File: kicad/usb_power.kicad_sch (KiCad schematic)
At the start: 12 parts, among them J1 12402012E212A, U6 TLV73333PDBV, U7 TLV73325PDBV

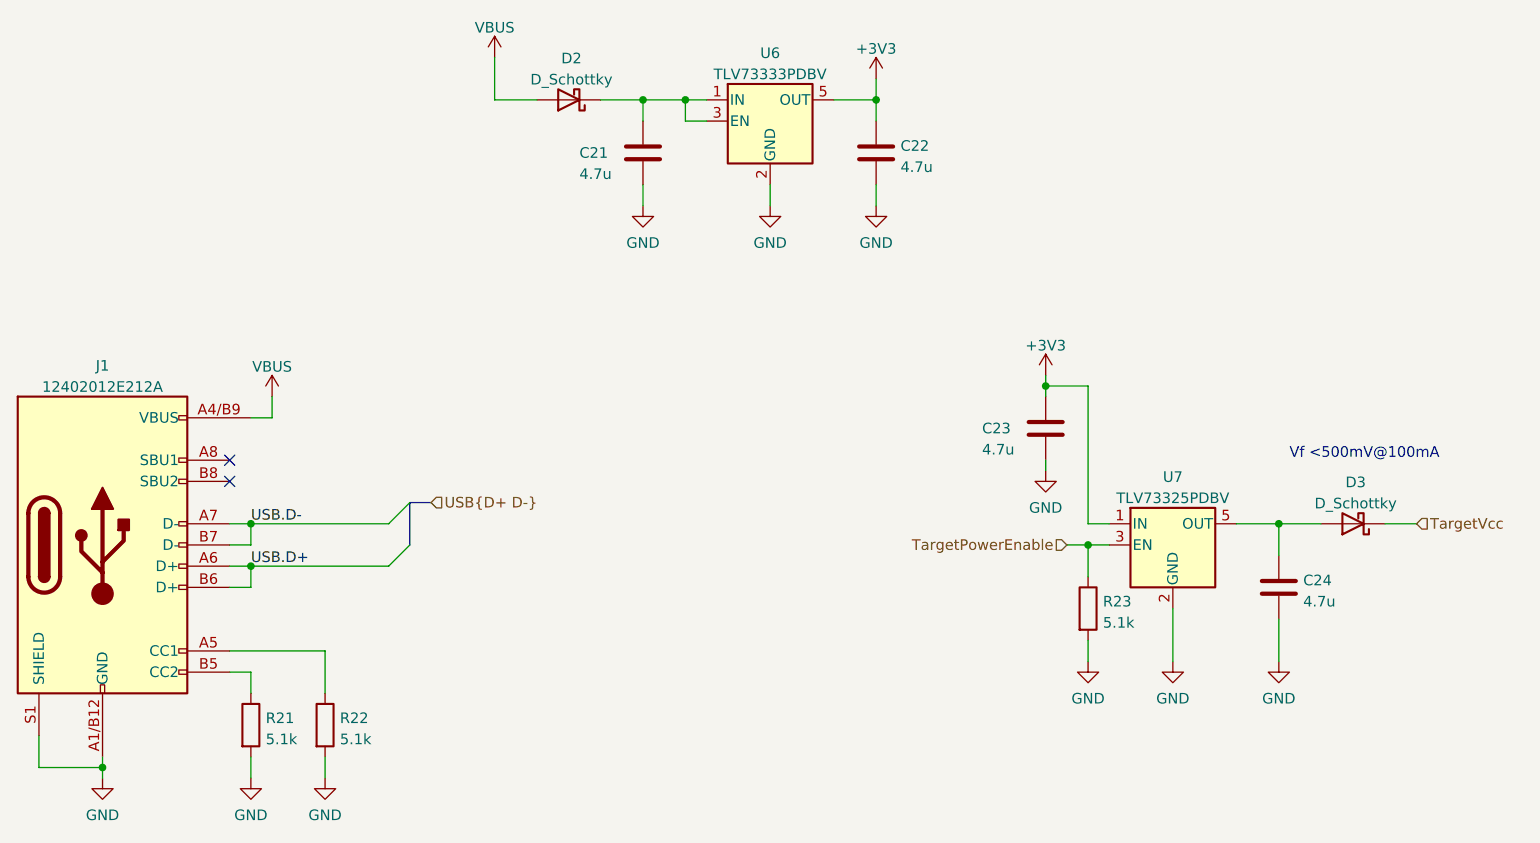
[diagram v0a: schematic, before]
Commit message: add fourth level converter for simultaneous programming + TX/RX
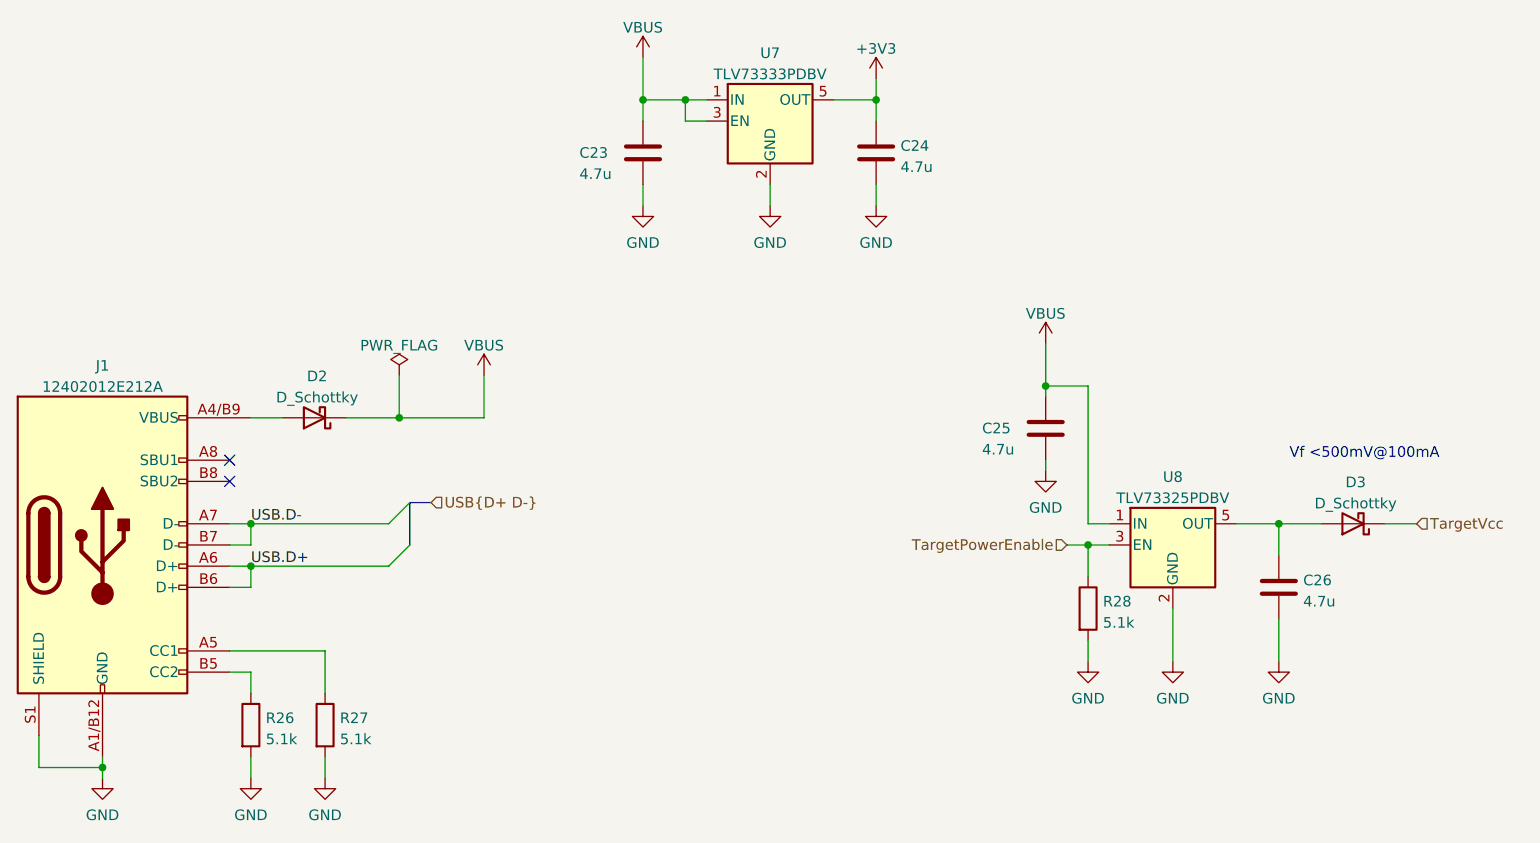
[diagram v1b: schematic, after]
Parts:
- U7: renamed from U6; symbol Regulator_Linear:TLV73333PDBV -> riotee:TLV73333PDBV
- U8: renamed from U7; symbol Regulator_Linear:TLV73325PDBV -> riotee:TLV73325PDBV
- renumbered C21 to C23, C22 to C24, C23 to C25, C24 to C26, R21 to R26, R22 to R27, R23 to R28
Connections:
- net +3V3: no longer C25.1, U8.1 (IN)
- net VBUS: now also C23.1, C25.1, D2.1 (K), U7.1 (IN), U7.3 (EN), U8.1 (IN); no longer D2.2 (A), J1.A4/B9 (VBUS), J1.B4/A9 (VBUS)
- new net: D2.2 (A), J1.A4/B9 (VBUS), J1.B4/A9 (VBUS)
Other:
- moved on the sheet: D2

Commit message: replace target supply diode with analog switch
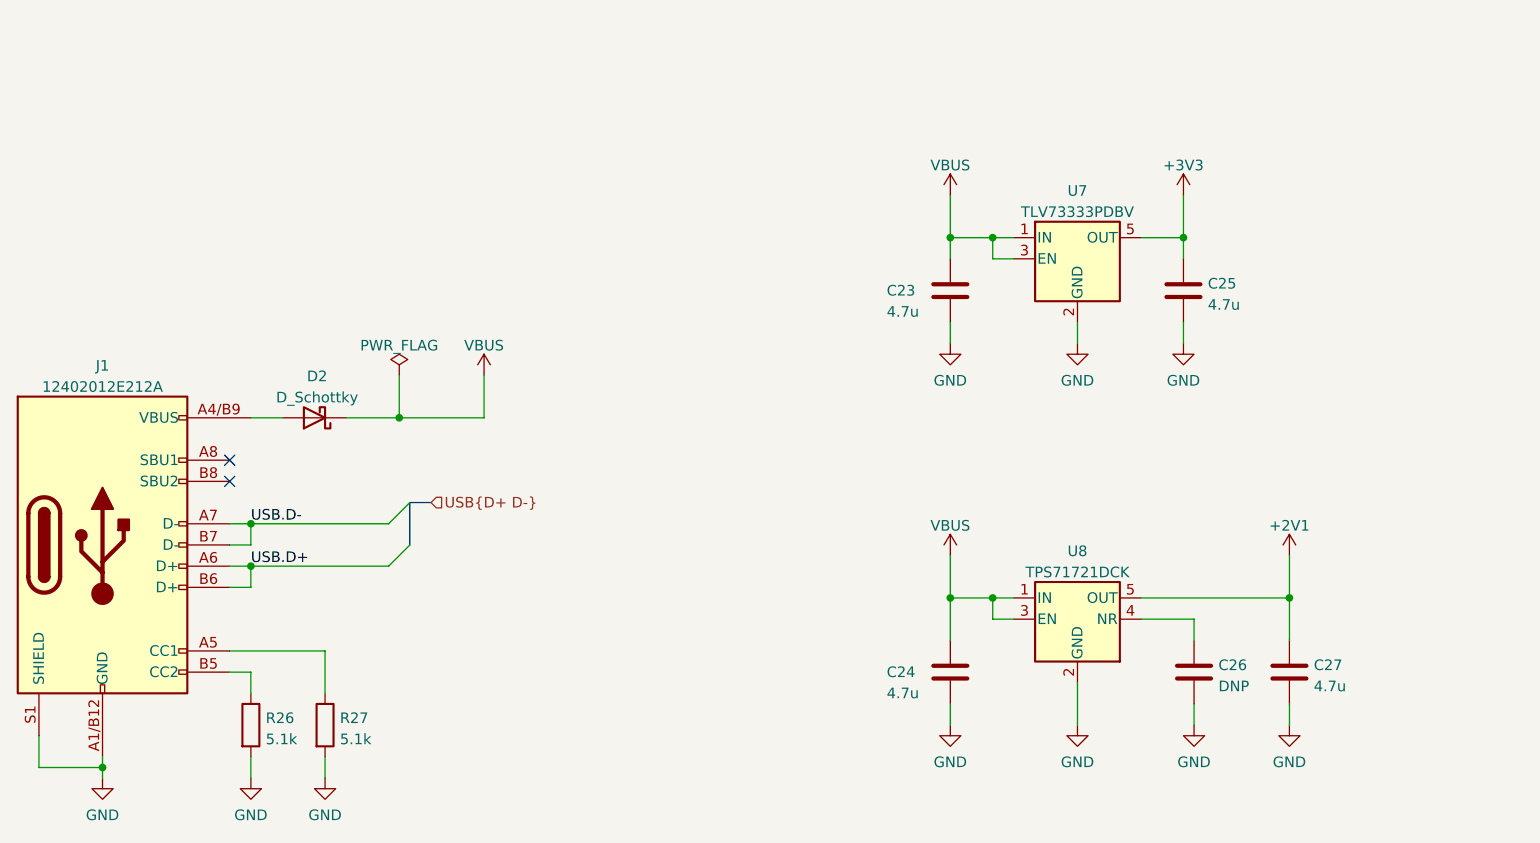
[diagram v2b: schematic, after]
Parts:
- removed D3: D_Schottky, Diode_SMD:D_SOD-523, symbol Device:D_Schottky
- removed R28: 5.1k, Resistor_SMD:R_0402_1005Metric, symbol Device:R
- removed U8: TLV73325PDBV, riotee:TI_DBV0005A, symbol riotee:TLV73325PDBV
- added C26: DNP, Capacitor_SMD:C_0402_1005Metric, symbol Device:C
- added U8: TPS71721DCK, riotee:TI_DCK0005A, symbol riotee:TPS71721DCK
- C23: MPN (none) -> CL05A475MP5NRNC
- C24: renamed from C25; MPN (none) -> CL05A475MP5NRNC
- C25: renamed from C24; MPN (none) -> CL05A475MP5NRNC
- C27: renamed from C26; MPN (none) -> CL05A475MP5NRNC
- D2: MPN (none) -> RB521S30T1G
- J1: MPN (none) -> 12402012E212A
- R26, R27: MPN (none) -> CR0402-FX-5101GLF
- U7: MPN (none) -> TLV73333PDBV
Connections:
- net GND: now also C26.2, U8.2 (GND)
- net VBUS: now also U8.1 (IN), U8.3 (EN)
- net +2V1: now reaches C27.1
- net +2V1: now also U8.5 (OUT)
- new net: C26.1, U8.4 (NR)
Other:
- note removed: "Vf <500mV@100mA"
- moved on the sheet: C23, C24, C25, C27, U7

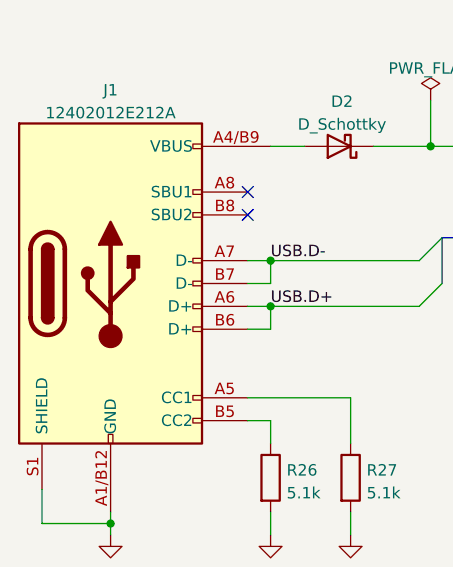
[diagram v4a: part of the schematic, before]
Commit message: migrate project to kicad 7
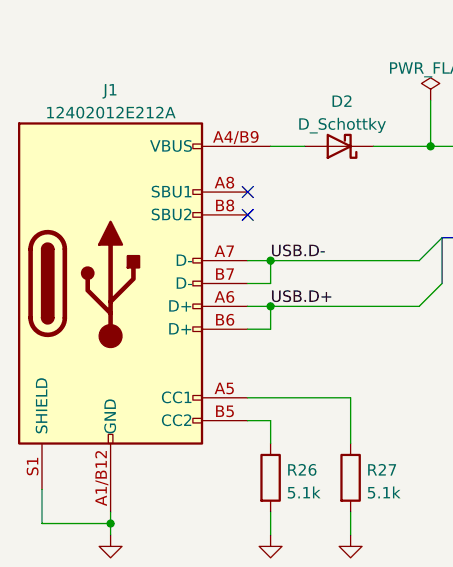
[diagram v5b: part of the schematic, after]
